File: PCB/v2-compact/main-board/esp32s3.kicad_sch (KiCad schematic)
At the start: 0 parts

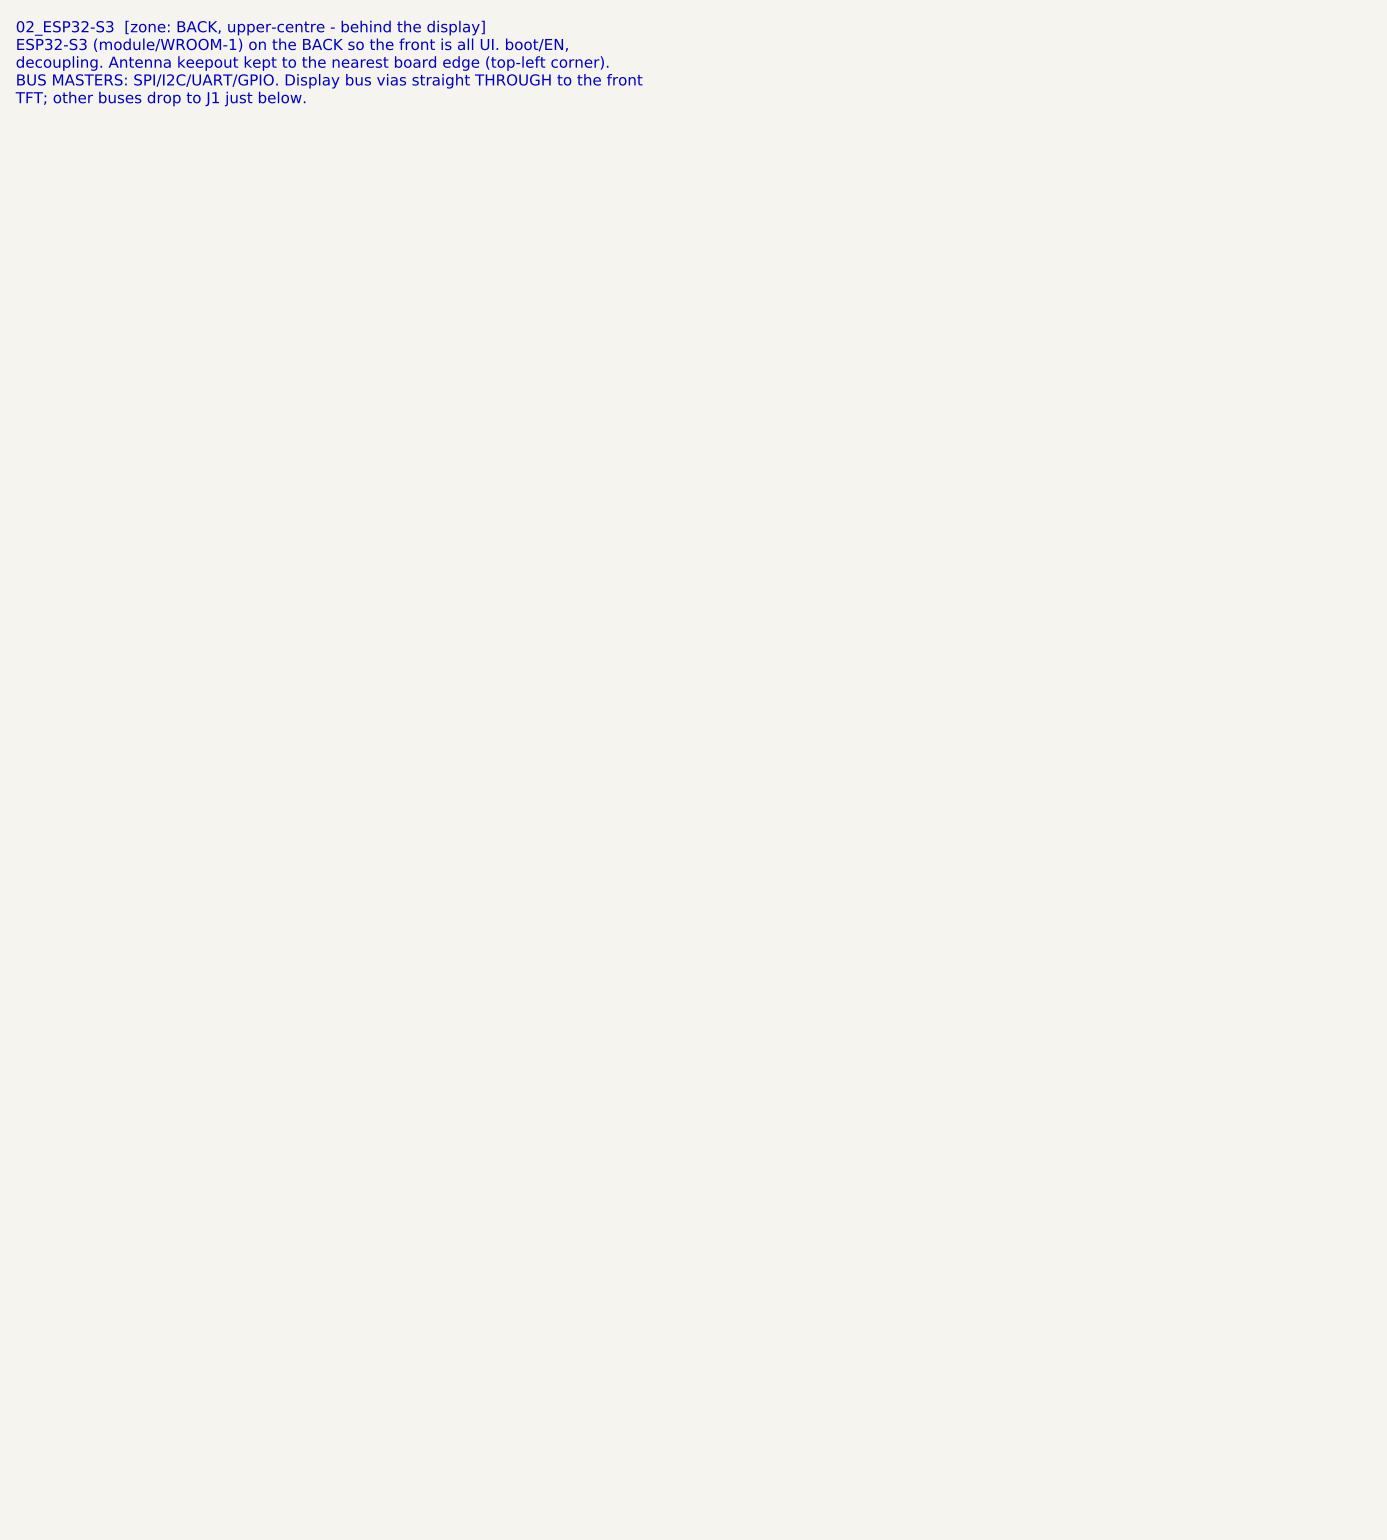
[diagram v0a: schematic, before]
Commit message: Schematics: main board ESP32-S3, microSD, and display/UI sheets
- 02_ESP32-S3: the brain. Shared SPI (LCD_SCK/MOSI + SD_MISO) for TFT and
  microSD, USB data to the USB-C through the ESD, and the full J1 interface to
  the shield (C5 UART + DRDY, I2C to PN532, RV1106 UART, IR, 1-Wire). EN/boot RC
  + decoupling.
- 04_microSD: SPI-mode card with CS pull-up + decoupling.
- 03_Display_UI: SPI TFT header, five nav buttons to GND, two status LEDs.

Netlist-verified: the S3 ties in the other end of every J1 net (isolated labels
on the main board dropped from 12 to 1).
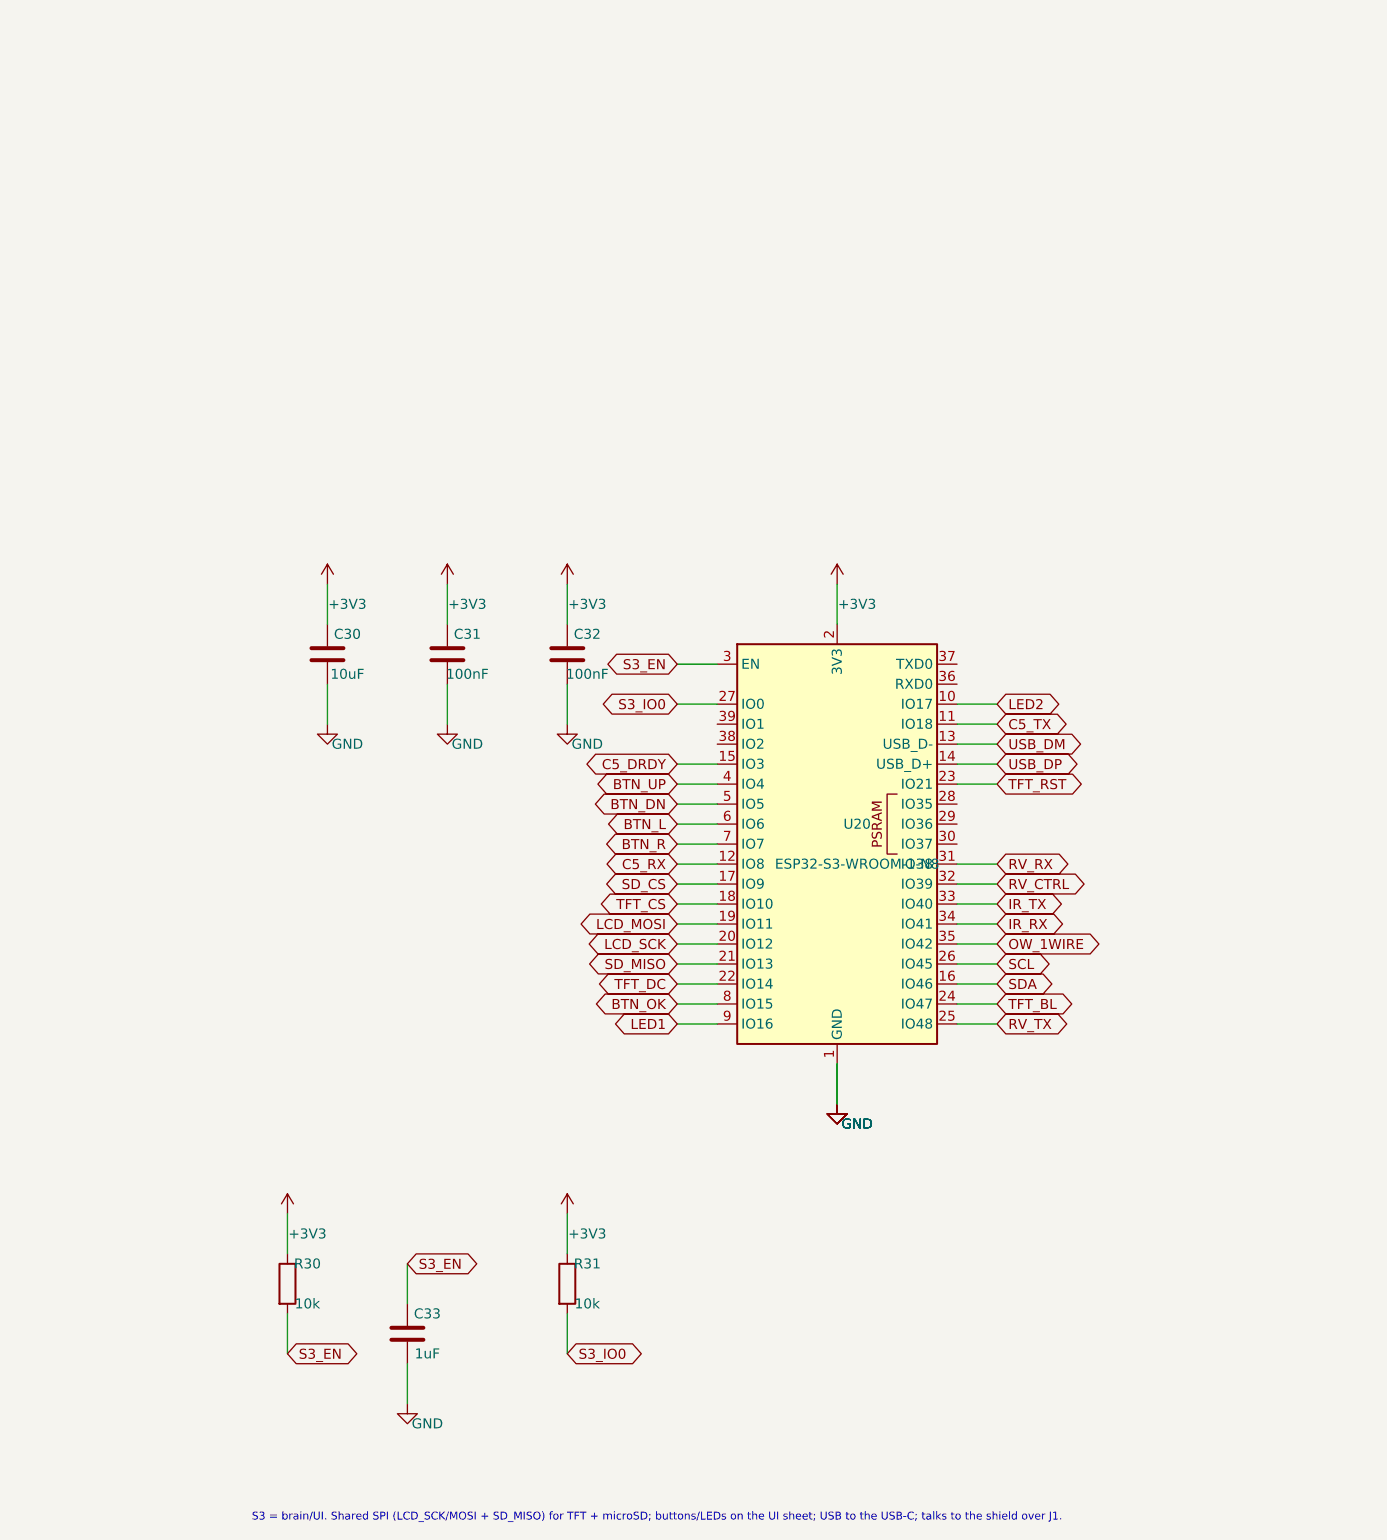
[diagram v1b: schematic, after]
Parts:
- added C30: 10uF, Capacitor_SMD:C_0402_1005Metric, symbol Device:C
- added C31, C32: 100nF, Capacitor_SMD:C_0402_1005Metric, symbol Device:C
- added C33: 1uF, Capacitor_SMD:C_0402_1005Metric, symbol Device:C
- added R30, R31: 10k, Resistor_SMD:R_0402_1005Metric, symbol Device:R
- added U20: ESP32-S3-WROOM-1-N8, RF_Module:ESP32-S3-WROOM-1, symbol RF_Module:ESP32-S3-WROOM-1
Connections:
- new net +3V3: C30.1, C31.1, C32.1, R30.1, R31.1, U20.2 (3V3)
- new net BTN_DN: U20.5 (IO5)
- new net BTN_L: U20.6 (IO6)
- new net BTN_OK: U20.8 (IO15)
- new net BTN_R: U20.7 (IO7)
- new net BTN_UP: U20.4 (IO4)
- new net C5_DRDY: U20.15 (IO3)
- new net C5_RX: U20.12 (IO8)
- new net C5_TX: U20.11 (IO18)
- new net GND: C30.2, C31.2, C32.2, C33.2, U20.1 (GND), U20.40 (GND), U20.41 (GND)
- new net IR_RX: U20.34 (IO41)
- new net IR_TX: U20.33 (IO40)
- new net LCD_MOSI: U20.19 (IO11)
- new net LCD_SCK: U20.20 (IO12)
- new net LED1: U20.9 (IO16)
- new net LED2: U20.10 (IO17)
- new net OW_1WIRE: U20.35 (IO42)
- new net RV_CTRL: U20.32 (IO39)
- new net RV_RX: U20.31 (IO38)
- new net RV_TX: U20.25 (IO48)
- new net S3_EN: C33.1, R30.2, U20.3 (EN)
- new net S3_IO0: R31.2, U20.27 (IO0)
- new net SCL: U20.26 (IO45)
- new net SDA: U20.16 (IO46)
- new net SD_CS: U20.17 (IO9)
- new net SD_MISO: U20.21 (IO13)
- new net TFT_BL: U20.24 (IO47)
- new net TFT_CS: U20.18 (IO10)
- new net TFT_DC: U20.22 (IO14)
- new net TFT_RST: U20.23 (IO21)
- new net USB_DM: U20.13 (USB_D-)
- new net USB_DP: U20.14 (USB_D+)
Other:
- note added: "S3 = brain/UI. Shared SPI (LCD_SCK/MOSI + SD_MISO) for TFT + microSD; buttons/LEDs on the UI sheet; USB to the USB-C; talks to the shield over J1."
- note removed: "02_ESP32-S3 [zone: BACK, upper-centre - behind the display] ESP32-S3 (module/WROOM-1) on the BACK so the front is all UI. boot/EN, decoupling. Antenna keepout kept to the nearest board edge (top-left corner). BUS MASTERS: SPI/I2C/UART/GPIO. Display bus vias straight THROUGH to the front TFT; other buses drop to J1 just below."
